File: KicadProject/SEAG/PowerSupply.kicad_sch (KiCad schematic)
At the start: 2 parts, among them U1 LM317_TO-220

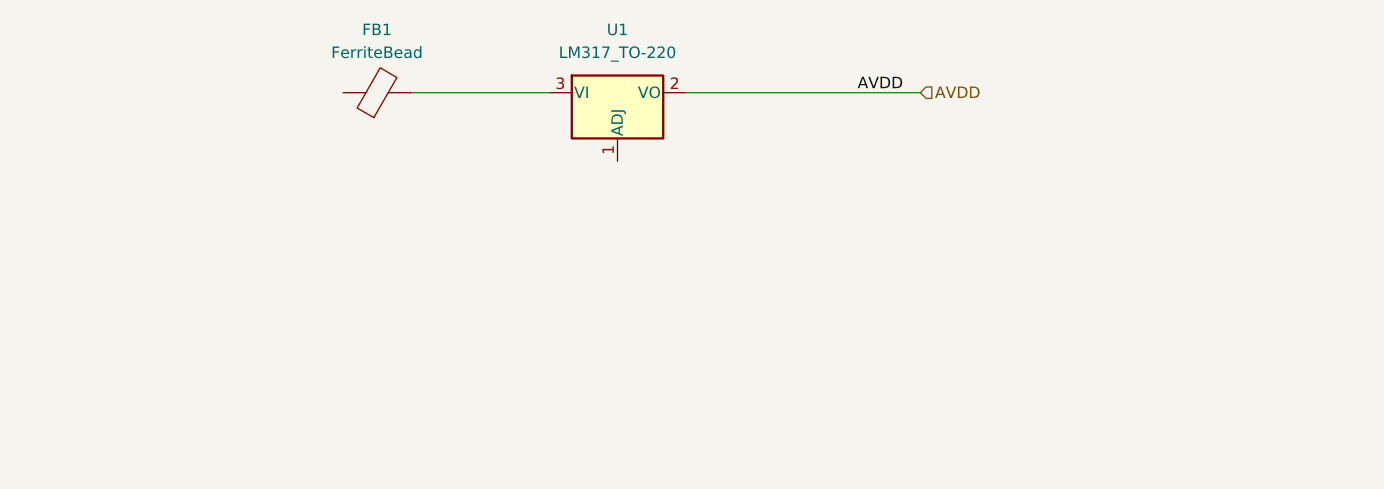
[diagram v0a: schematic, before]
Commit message: Added power supply and serial link header to PCB schematic
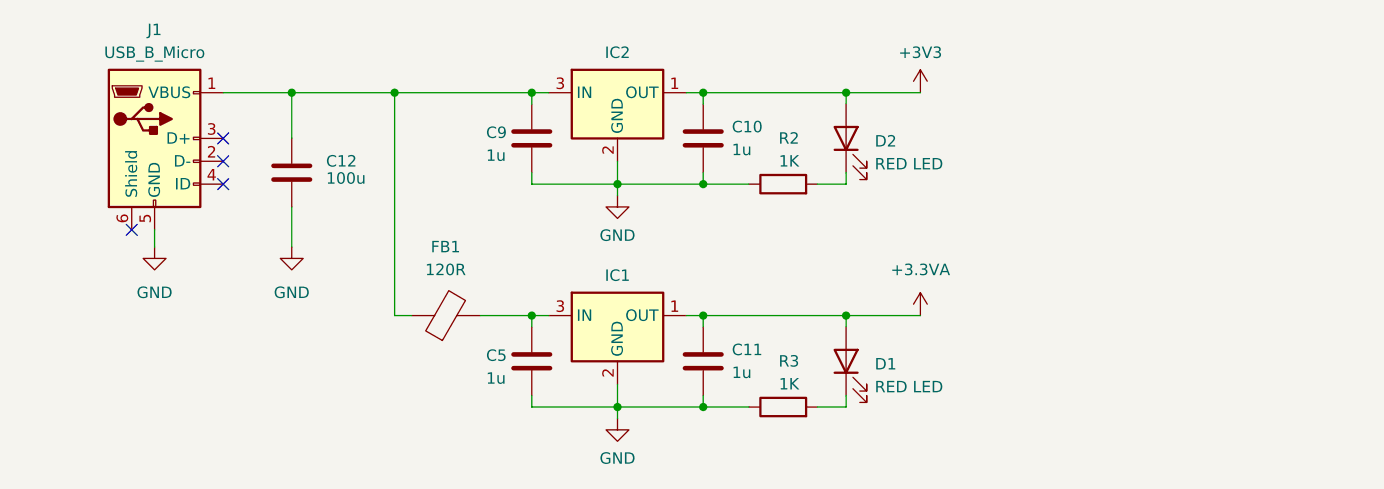
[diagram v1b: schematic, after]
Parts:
- removed U1: LM317_TO-220, Package_TO_SOT_THT:TO-220-3_Vertical, symbol Regulator_Linear:LM317_TO-220
- added C10, C11, C5, C9: 1u, symbol Device:C
- added C12: 100u, symbol Device:C
- added D1, D2: RED LED, symbol Device:LED
- added IC1, IC2: ~, MyLibrary:AP736533YG13, symbol MyLibrary:AP7365-33YG-13
- added J1: USB_B_Micro, symbol Connector:USB_B_Micro
- added R2, R3: 1K, symbol Device:R
- FB1: value FerriteBead -> 120R; footprint (none) -> Inductor_SMD:L_0805_2012Metric
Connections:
- net at FB1.1: now also C12.1, C9.1, IC2.3 (IN), J1.1 (VBUS)
- net at FB1.2: now also C5.1, IC1.3 (IN)
- new net: D1.1 (K), R3.2
- new net: D2.1 (K), R2.2
- new net +3.3VA: C11.1, D1.2 (A), IC1.1 (OUT)
- new net +3V3: C10.1, D2.2 (A), IC2.1 (OUT)
- new net GND: C10.2, C11.2, C12.2, C5.2, C9.2, IC1.2 (GND), IC1.4 (GND), IC2.2 (GND), IC2.4 (GND), J1.5 (GND), R2.1, R3.1
- no-connect marks 0 -> 4
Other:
- title: (none) -> Power Supply

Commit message: Added 'AudioFiltering' and 'Codec' sheets to PCB schematic, started PCB layout with decouple caps and MCU. The codec in sheet 'Codec' is wrong, placed for testing
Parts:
- C10, C11, C12, C5, C9: footprint (none) -> Capacitor_SMD:C_0805_2012Metric
- D1, D2: footprint (none) -> LED_SMD:LED_0805_2012Metric
- R2, R3: footprint (none) -> Resistor_SMD:R_0805_2012Metric
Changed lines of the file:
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@@
       (effects (font (size 1.27 1.27)) (justify left))
     )
-    (property "Footprint" "" (at 72.7202 41.275 0)
+    (property "Footprint" "Capacitor_SMD:C_0805_2012Metric" (at 72.7202 41.275 0)
       (effects (font (size 1.27 1.27)) hide)
     )
@@
       (effects (font (size 1.27 1.27)) (justify left))
     )
-    (property "Footprint" "" (at 46.0502 45.085 0)
+    (property "Footprint" "Capacitor_SMD:C_0805_2012Metric" (at 46.0502 45.085 0)
       (effects (font (size 1.27 1.27)) hide)
     )
@@
       (effects (font (size 1.27 1.27)) (justify left))
     )
-    (property "Footprint" "" (at 72.7202 66.04 0)
+    (property "Footprint" "Capacitor_SMD:C_0805_2012Metric" (at 72.7202 66.04 0)
       (effects (font (size 1.27 1.27)) hide)
     )
@@
       (effects (font (size 1.27 1.27)) (justify left))
     )
-    (property "Footprint" "" (at 91.7702 41.275 0)
+    (property "Footprint" "Capacitor_SMD:C_0805_2012Metric" (at 91.7702 41.275 0)
       (effects (font (size 1.27 1.27)) hide)
     )
@@
       (effects (font (size 1.27 1.27)) (justify left))
     )
-    (property "Footprint" "" (at 91.7702 66.04 0)
+    (property "Footprint" "Capacitor_SMD:C_0805_2012Metric" (at 91.7702 66.04 0)
       (effects (font (size 1.27 1.27)) hide)
     )
@@
       (effects (font (size 1.27 1.27)) (justify right))
     )
-    (property "Footprint" "" (at 106.68 62.23 0)
+    (property "Footprint" "LED_SMD:LED_0805_2012Metric" (at 106.68 62.23 0)
       (effects (font (size 1.27 1.27)) hide)
     )
@@
       (effects (font (size 1.27 1.27)))
     )
-    (property "Footprint" "" (at 99.695 69.088 90)
+    (property "Footprint" "Resistor_SMD:R_0805_2012Metric" (at 99.695 69.088 90)
       (effects (font (size 1.27 1.27)) hide)
     )
@@
       (effects (font (size 1.27 1.27)) (justify right))
     )
-    (property "Footprint" "" (at 106.68 37.465 0)
+    (property "Footprint" "LED_SMD:LED_0805_2012Metric" (at 106.68 37.465 0)
       (effects (font (size 1.27 1.27)) hide)
     )
@@
       (effects (font (size 1.27 1.27)))
     )
-    (property "Footprint" "" (at 99.695 44.323 90)
-      (effects (font (size 1.27 1.27)) hide)
-    )
+    (property "Footprint" "Resistor_SMD:R_0805_2012Metric" (at 99.695 44.323 90)
+      (effects (font (size 1.27 1.27)) hide)
+    )

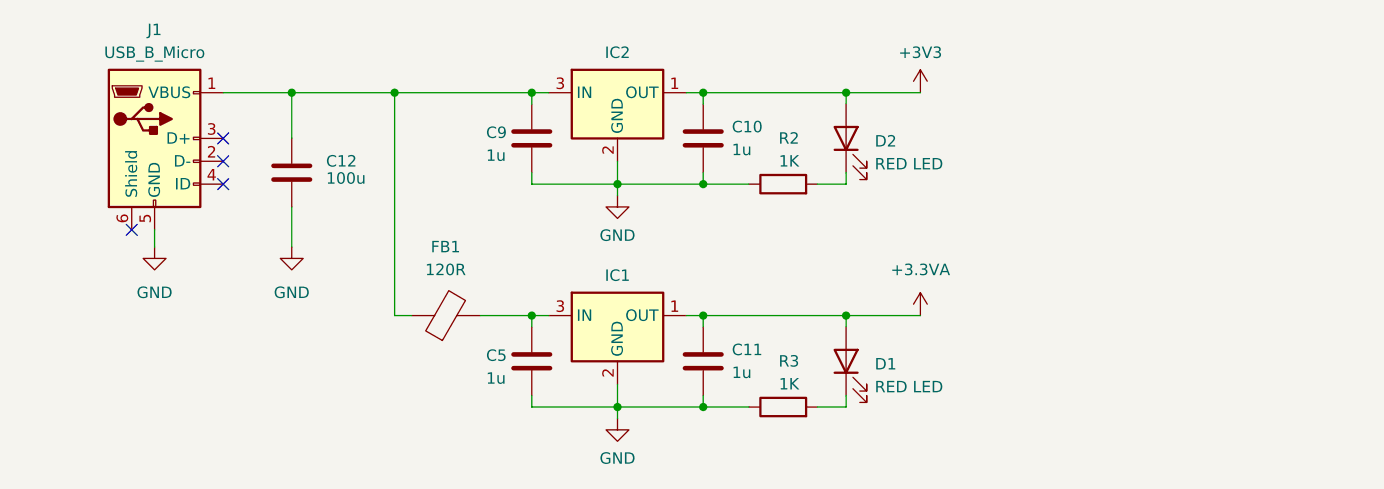
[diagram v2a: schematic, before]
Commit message: Added ESD protection, extra filtering with ferrite bead
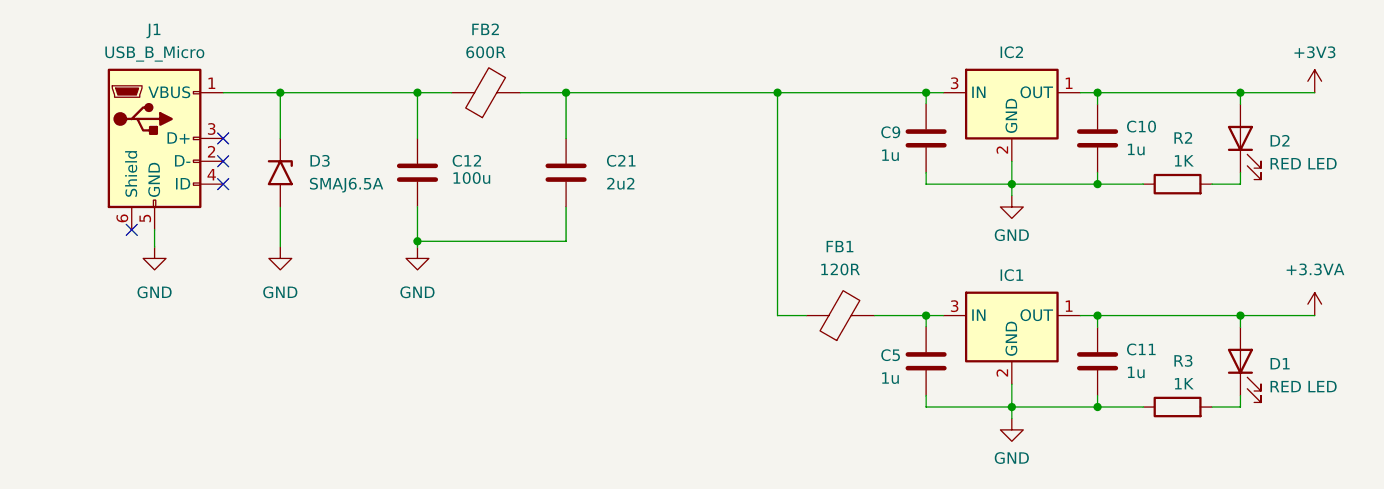
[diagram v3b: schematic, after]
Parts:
- added C21: 2u2, symbol Device:C
- added D3: SMAJ6.5A, Diode_SMD:D_SMA, symbol Diode:SMAJ6.5A
- added FB2: 600R, Inductor_SMD:L_0805_2012Metric, symbol Device:FerriteBead
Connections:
- net GND: now also C21.2, D3.2 (A2)
- net at C9.1, FB1.1, IC2.3 (IN): now also C21.1, FB2.2; no longer C12.1, J1.1 (VBUS)
- new net: C12.1, D3.1 (A1), FB2.1, J1.1 (VBUS)
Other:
- moved on the sheet: C10, C11, C12, C5, C9, D1, D2, FB1, IC1, IC2, R2, R3

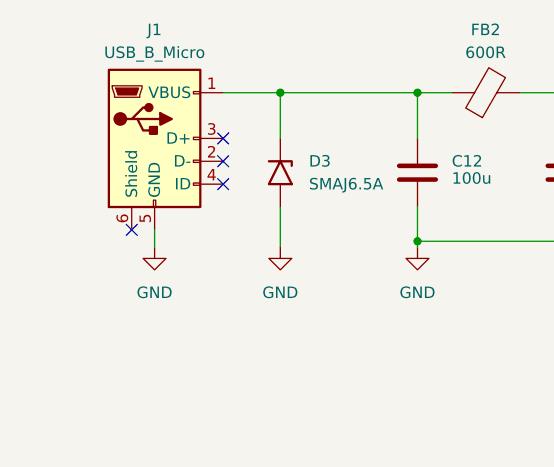
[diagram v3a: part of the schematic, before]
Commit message: Finished PCB, stil uncertain about couple things
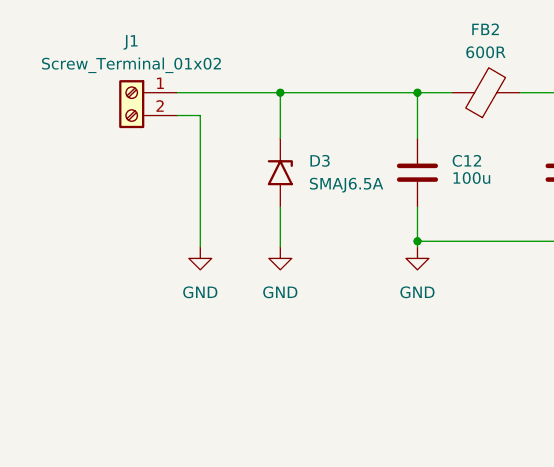
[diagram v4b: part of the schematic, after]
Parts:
- removed J1: USB_B_Micro, symbol Connector:USB_B_Micro
- added J1: Screw_Terminal_01x02, TerminalBlock_Phoenix:TerminalBlock_Phoenix_MKDS-1,5-2_1x02_P5.00mm_Horizontal, symbol Connector:Screw_Terminal_01x02
- C21: footprint (none) -> Capacitor_SMD:C_0805_2012Metric
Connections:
- net GND: now also J1.2 (Pin_2)
- net at C12.1, D3.1 (A1), FB2.1: now also J1.1 (Pin_1)
- no-connect marks 4 -> 0

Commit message: PCB rev 2
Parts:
- renumbered C12 to C201, C21 to C202, C9 to C203, C10 to C204, C5 to C205, C11 to C206, R2 to R201, R3 to R202
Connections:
- net GND: now also R202.2; no longer R202.1
- net at D1.1 (K): now also R202.1; no longer R202.2
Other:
- moved on the sheet: D1, D2, R201, R202

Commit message: Slight PCB changes
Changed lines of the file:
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@@
   (symbol (lib_id "Device:R") (at 144.78 67.31 270) (mirror x) (unit 1)
     (in_bom yes) (on_board yes) (dnp no)
-    (property "Reference" "R202" (at 144.145 62.23 90)
+    (property "Reference" "R202" (at 145.415 62.23 90)
       (effects (font (size 1.27 1.27)))
     )
-    (property "Value" "1K" (at 144.145 64.77 90)
+    (property "Value" "1K" (at 145.415 64.77 90)
       (effects (font (size 1.27 1.27)))
     )
